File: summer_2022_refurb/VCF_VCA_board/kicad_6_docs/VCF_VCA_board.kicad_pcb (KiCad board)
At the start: 2 copper layers, 132.1 x 185.4 mm, 171 parts, among them J1 VCO_port, J2 ext_port, J3 mod_osc_port, J4 S&H_port, J5 ADSR_port, J6 ribbon_port, J7 power_entry, SW1 SR1712F-0204, SW2 SR1712F-0204, SW3 series_parallel_switch, SW401 SW_SPDT_center_off, U1 TL072, U10 SSI2164, U11 SSI2164, U2 TL072, U3 TL072, U4 TL072, U5 TL072, U501 LM4040DBZ-5, U502 LM4040DBZ-5, U6 TL072, U7 TL072, U8 TL072, U9 TL072

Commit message: Change directory structure, minor schem and pcb tweaks
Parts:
- renumbered C601 to C401, C602 to C402, C603 to C403, C604 to C404, C605 to C405, C401 to C501, C402 to C502, C403 to C503, C404 to C504, C405 to C505, C501 to C601, C502 to C602, C503 to C603, C504 to C604, C505 to C605, C506 to C606, C507 to C607, C508 to C608, C509 to C609, C510 to C610, C511 to C611, C512 to C612, C513 to C613, C514 to C614, C515 to C615, C516 to C616, C517 to C617, C518 to C618, C519 to C619, C520 to C620, C521 to C621, C522 to C622, C523 to C623, C524 to C624, C525 to C625, C526 to C626, D601 to D401, D602 to D402, D401 to D501, D402 to D502, D403 to D503, D404 to D504, R601 to R401, R602 to R402, R603 to R403, R604 to R404, R605 to R405, R606 to R406, R607 to R407, R608 to R408, R609 to R409, R610 to R410, R611 to R411, R401 to R501, R402 to R502, R403 to R503, R404 to R504, R405 to R505, R406 to R506, R407 to R507, R408 to R508, R409 to R509, R410 to R510, R411 to R511, R412 to R512, R413 to R513, R414 to R514, R415 to R515, R416 to R516, R417 to R517, R418 to R518, R419 to R519, R420 to R520, R421 to R521, R422 to R522, R423 to R523, R424 to R524, R501 to R601, R502 to R602, RV401 to RV501, RV402 to RV502, RV403 to RV503, RV404 to RV504, RV405 to RV505, RV406 to RV506, RV407 to RV507, RV408 to RV508, RV409 to RV509, RV410 to RV510, RV411 to RV511, SW401 to SW501, U501 to U601, U502 to U602
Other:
- board text added: "Filter and VCA board rev 0 2022-06-16"
- board text removed: "Filter and VCA board rev 0 2022-06-15"

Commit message: Add cool kibuzzard labels, minor tweaks
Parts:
- added REF**: OSHW-Logo_5.7x6mm_SilkScreen, Symbol:OSHW-Logo_5.7x6mm_SilkScreen, B.Cu at (117.1, 176.5)
- added kibuzzard-62AC755C: G***, kibuzzard-62AC755C, B.Cu at (138.4, 104.1)
- added kibuzzard-62AC755C: G***, kibuzzard-62AC755C, B.Cu at (138.4, 144.8)
- added kibuzzard-62AC755C: G***, kibuzzard-62AC755C, B.Cu at (138.4, 163.8)
- added kibuzzard-62AC755C: G***, kibuzzard-62AC755C, B.Cu at (39.4, 158.1)
- added kibuzzard-62AC755C: G***, kibuzzard-62AC755C, B.Cu at (34.3, 17.8)
- added kibuzzard-62AC755C: G***, kibuzzard-62AC755C, B.Cu at (138.4, 15.2)
- added kibuzzard-62AC755C: G***, kibuzzard-62AC755C, B.Cu at (138.4, 67.3)
- added kibuzzard-62AC755C: G***, kibuzzard-62AC755C, B.Cu at (57.1, 168.9)
- added kibuzzard-62AC755C: G***, kibuzzard-62AC755C, B.Cu at (138.4, 20.3)
- added kibuzzard-62AC78CB: G***, kibuzzard-62AC78CB, B.Cu at (57.1, 182.9)
- added kibuzzard-62AC791A: G***, kibuzzard-62AC791A, B.Cu at (62.2, 168.9)
- added kibuzzard-62AC791A: G***, kibuzzard-62AC791A, B.Cu at (81.3, 154.3)
- added kibuzzard-62AC792A: G***, kibuzzard-62AC792A, B.Cu at (52.1, 168.9)
- added kibuzzard-62AC792A: G***, kibuzzard-62AC792A, B.Cu at (87.6, 154.3)
- added kibuzzard-62AC7A9F: G***, kibuzzard-62AC7A9F, B.Cu at (116.8, 170.8)
- added kibuzzard-62AC8760: G***, kibuzzard-62AC8760, B.Cu at (126.4, 176.5)
- added kibuzzard-62AC886F: G***, kibuzzard-62AC886F, B.Cu at (135.9, 137.2)
- added kibuzzard-62AC887D: G***, kibuzzard-62AC887D, B.Cu at (135.9, 139.7)
- added kibuzzard-62AC8892: G***, kibuzzard-62AC8892, B.Cu at (137.8, 142.2)
- added kibuzzard-62AC88AD: G***, kibuzzard-62AC88AD, B.Cu at (137.2, 161.3)
- added kibuzzard-62AC88C6: G***, kibuzzard-62AC88C6, B.Cu at (137.2, 101.6)
- added kibuzzard-62AC88DA: G***, kibuzzard-62AC88DA, B.Cu at (139.1, 62.2)
- added kibuzzard-62AC88EB: G***, kibuzzard-62AC88EB, B.Cu at (136.5, 64.8)
- added kibuzzard-62AC8908: G***, kibuzzard-62AC8908, B.Cu at (137.8, 17.8)
- added kibuzzard-62AC892A: G***, kibuzzard-62AC892A, B.Cu at (34.9, 12.7)
- added kibuzzard-62AC892A: G***, kibuzzard-62AC892A, B.Cu at (138.4, 12.7)
- added kibuzzard-62AC8951: G***, kibuzzard-62AC8951, B.Cu at (35.6, 15.2)
- added kibuzzard-62AC8974: G***, kibuzzard-62AC8974, B.Cu at (22.9, 15.2)
- added kibuzzard-62AC8994: G***, kibuzzard-62AC8994, B.Cu at (149.9, 162.6)
- added kibuzzard-62AC89A8: G***, kibuzzard-62AC89A8, B.Cu at (149.9, 141.0)
- added kibuzzard-62AC89C0: G***, kibuzzard-62AC89C0, B.Cu at (149.9, 102.9)
- added kibuzzard-62AC89D1: G***, kibuzzard-62AC89D1, B.Cu at (149.9, 64.8)
- added kibuzzard-62AC89EA: G***, kibuzzard-62AC89EA, B.Cu at (149.9, 16.5)
- added kibuzzard-62AC8A1C: G***, kibuzzard-62AC8A1C, B.Cu at (48.3, 102.2)
- added kibuzzard-62AC8A2D: G***, kibuzzard-62AC8A2D, B.Cu at (48.3, 112.4)
- added kibuzzard-62AC8A40: G***, kibuzzard-62AC8A40, B.Cu at (125.1, 69.8)
- added kibuzzard-62AC8A4C: G***, kibuzzard-62AC8A4C, B.Cu at (74.3, 69.8)
- added kibuzzard-62AC8A61: G***, kibuzzard-62AC8A61, B.Cu at (40.6, 50.8)
- added kibuzzard-62AC8A72: G***, kibuzzard-62AC8A72, B.Cu at (142.2, 50.8)
- added kibuzzard-62AC8A87: G***, kibuzzard-62AC8A87, B.Cu at (49.5, 23.5)
- added kibuzzard-62AC8A9A: G***, kibuzzard-62AC8A9A, B.Cu at (117.5, 10.8)
- added kibuzzard-62AC8ACE: G***, kibuzzard-62AC8ACE, B.Cu at (92.1, 21.6)
- added kibuzzard-62AC8AE3: G***, kibuzzard-62AC8AE3, B.Cu at (77.5, 21.6)
- added kibuzzard-62AC8B01: G***, kibuzzard-62AC8B01, B.Cu at (66.7, 99.1)
- added kibuzzard-62AC8B15: G***, kibuzzard-62AC8B15, B.Cu at (106.0, 99.1)
- added kibuzzard-62AC8B2D: G***, kibuzzard-62AC8B2D, B.Cu at (57.8, 132.1)
- added kibuzzard-62AC8B47: G***, kibuzzard-62AC8B47, B.Cu at (114.9, 132.1)
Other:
- board text removed: "+5V REF"
- board text removed: "-5V REF"
- board text removed: "1v/oct trim A"
- board text removed: "1v/oct trim B"
- board text removed: "ADSR BOARD PORT"
- board text removed: "AUDIO I"
- board text removed: "AUDIO O"
- board text removed: "CV A"
- board text removed: "CV B"
- board text removed: "DC POWER IN"
- board text removed: "DRY AUDIO"
- board text removed: "EXT CONN PORT"
- board text removed: "EXT CV I"
- board text removed: "Filter and VCA board rev 0 2022-06-16"
- board text removed: "GND"
- board text removed: "MOD OSC I"
- board text removed: "MODOSC BOARD PORT"
- board text removed: "Ox Ribbon Synth"
- board text removed: "RIBBON A I"
- board text removed: "RIBBON B I"
- board text removed: "RIBBON BOARD PORT"
- board text removed: "S&H BOARD PORT"
- board text removed: "S&H I"
- board text removed: "S&H MIXER I"
- board text removed: "V+"
- board text removed: "V-"
- board text removed: "VCA CV I"
- board text removed: "VCF A"
- board text removed: "VCF B"
- board text removed: "VCF ENV I"
- board text removed: "VCO BOARD PORT"
- board text removed: "VCO MOD I"
- board text removed: "WET AUDIO"
- board text removed: "base trim A"
- board text removed: "base trim B"
- board text removed: "notch reject trim A"
- board text removed: "notch reject trim B"

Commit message: Fix incorrect notch filter amp
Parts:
- removed RV202, RV302: 50k, Potentiometer_THT:Potentiometer_Bourns_3296W_Vertical
- removed kibuzzard-62AC8ACE: G***, kibuzzard-62AC8ACE
- removed kibuzzard-62AC8AE3: G***, kibuzzard-62AC8AE3
- added R210: 30k, Resistor_SMD:R_0805_2012Metric, B.Cu at (68.6, 26.7)
- added R211: 30k, Resistor_SMD:R_0805_2012Metric, B.Cu at (68.6, 22.9)
- added R212: 30k, Resistor_SMD:R_0805_2012Metric, B.Cu at (68.6, 19.1)
- added R310: 30k, Resistor_SMD:R_0805_2012Metric, B.Cu at (100.3, 27.9)
- added R311: 30k, Resistor_SMD:R_0805_2012Metric, B.Cu at (100.3, 24.1)
- added R312: 30k, Resistor_SMD:R_0805_2012Metric, B.Cu at (100.3, 20.3)
- renumbered R203 to R201, R201 to R202, R208 to R203, R213 to R204, R202 to R205, R204 to R206, R206 to R207, R205 to R208, R207 to R209, R210 to R213, R209 to R215, R217 to R216, R303 to R301, R301 to R302, R308 to R303, R313 to R304, R302 to R305, R304 to R306, R306 to R307, R305 to R308, R307 to R309, R310 to R313, R309 to R315, R317 to R316
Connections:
- U1 pad 2: /SVF_A/NOTCH_OUT -> Net-(U1-Pad2)
- U1 pad 3: Net-(RV202-Pad2) -> GND
- U6 pad 5: Net-(RV302-Pad2) -> GND
- U6 pad 6: /SVF_B/NOTCH_OUT -> Net-(U6-Pad6)
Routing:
- net /SVF_A/BP_OUT: track 120.3 -> 86.6 mm, vias 2 -> 1
- net /SVF_A/HP_OUT: track 64.8 -> 95.3 mm, vias 3 -> 4
- net /SVF_B/SIGNAL_IN: track 88.2 -> 58.8 mm
- net /SVF_B/BP_OUT: track 133.3 -> 106.1 mm, vias 2 -> 1
- net /SVF_A/SIGNAL_IN: track 167.5 -> 150.1 mm
- net Net-(U6-Pad6): track 0.00 -> 12.9 mm
- net Net-(U1-Pad2): track 0.00 -> 12.2 mm
- net /SVF_B/HP_OUT: track 90.5 -> 100.0 mm
- net /SVF_B/LP_OUT: track 57.5 -> 67.0 mm, vias 1 -> 2
- net /SVF_A/LP_OUT: track 31.8 -> 40.2 mm
- net Net-(RV202-Pad2): track 8.07 -> 0.00 mm
- net Net-(RV302-Pad2): track 7.94 -> 0.00 mm
- net /SVF_B/NOTCH_OUT: track 64.0 -> 66.8 mm
- net /SVF_A/NOTCH_OUT: track 66.7 -> 69.1 mm

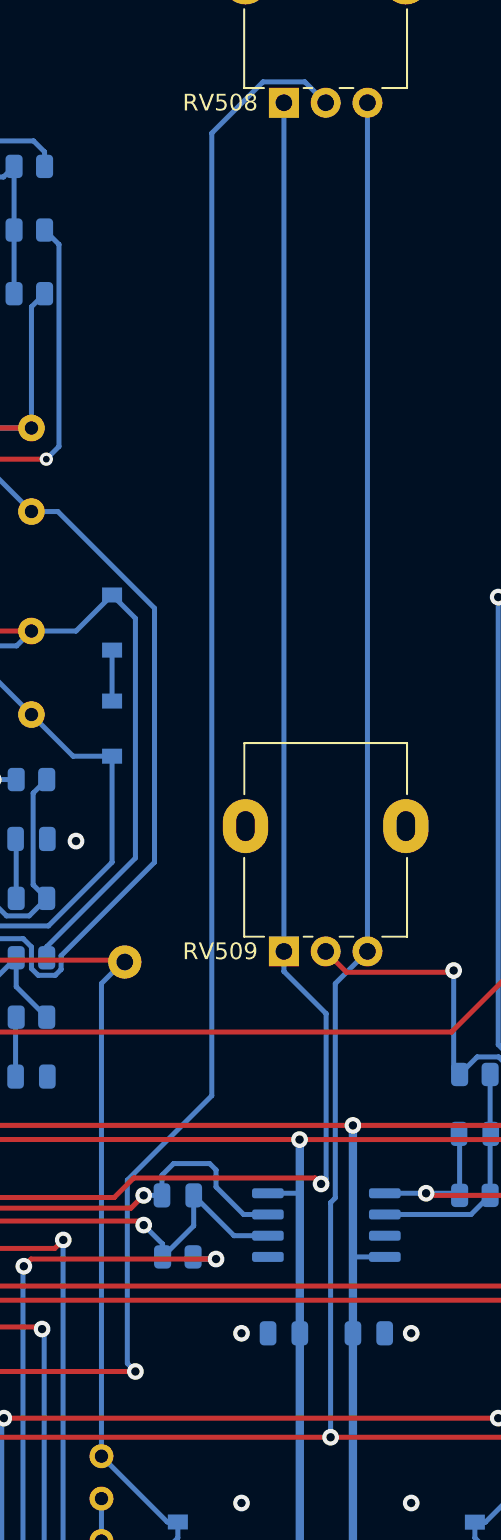
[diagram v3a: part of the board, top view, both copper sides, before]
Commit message: Fix rotation of separation pot, regenerate construction docs
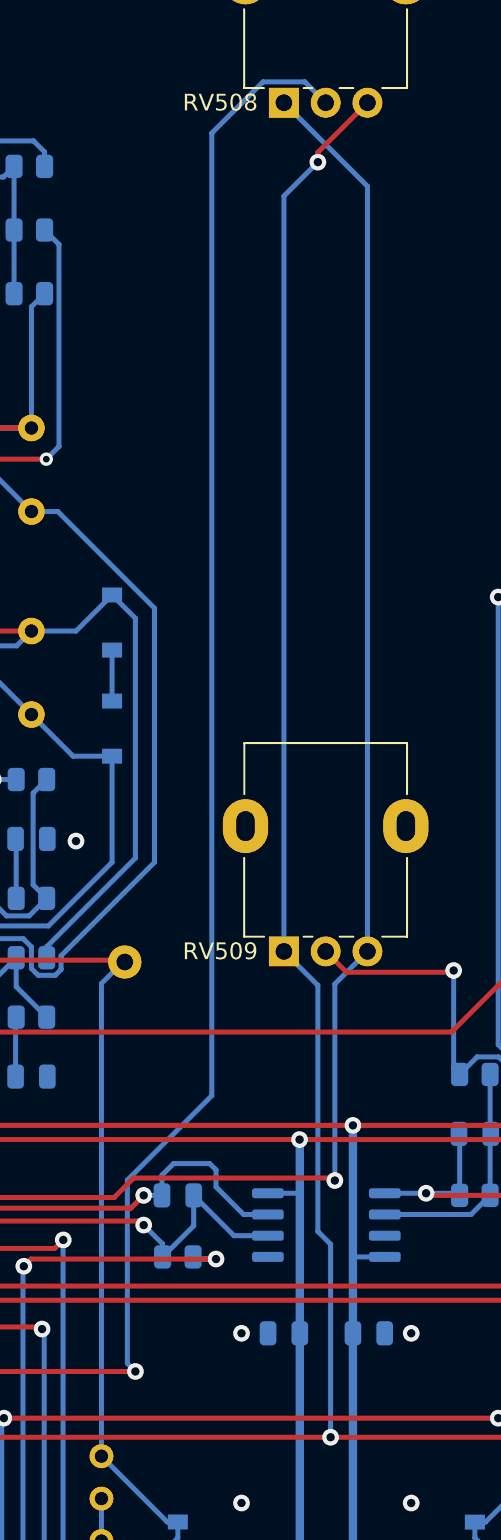
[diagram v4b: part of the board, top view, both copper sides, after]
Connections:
- RV509 pad 1: -5V REF -> +5V REF
- RV509 pad 3: +5V REF -> -5V REF
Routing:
- net +5V REF: track 202.9 -> 205.2 mm, vias 4 -> 5
- net -5V REF: track 224.3 -> 226.6 mm
